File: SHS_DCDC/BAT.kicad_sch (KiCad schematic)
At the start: 15 parts, among them Q10 PMV100XPEAR, Q11 PMV100XPEAR, Q12 PMV100XPEAR, Q13 PMV100XPEAR, Q17 PMV100XPEAR, Q9 PMV100XPEAR, U2 INA181, U7 MCP101, U9 BD49LxxG

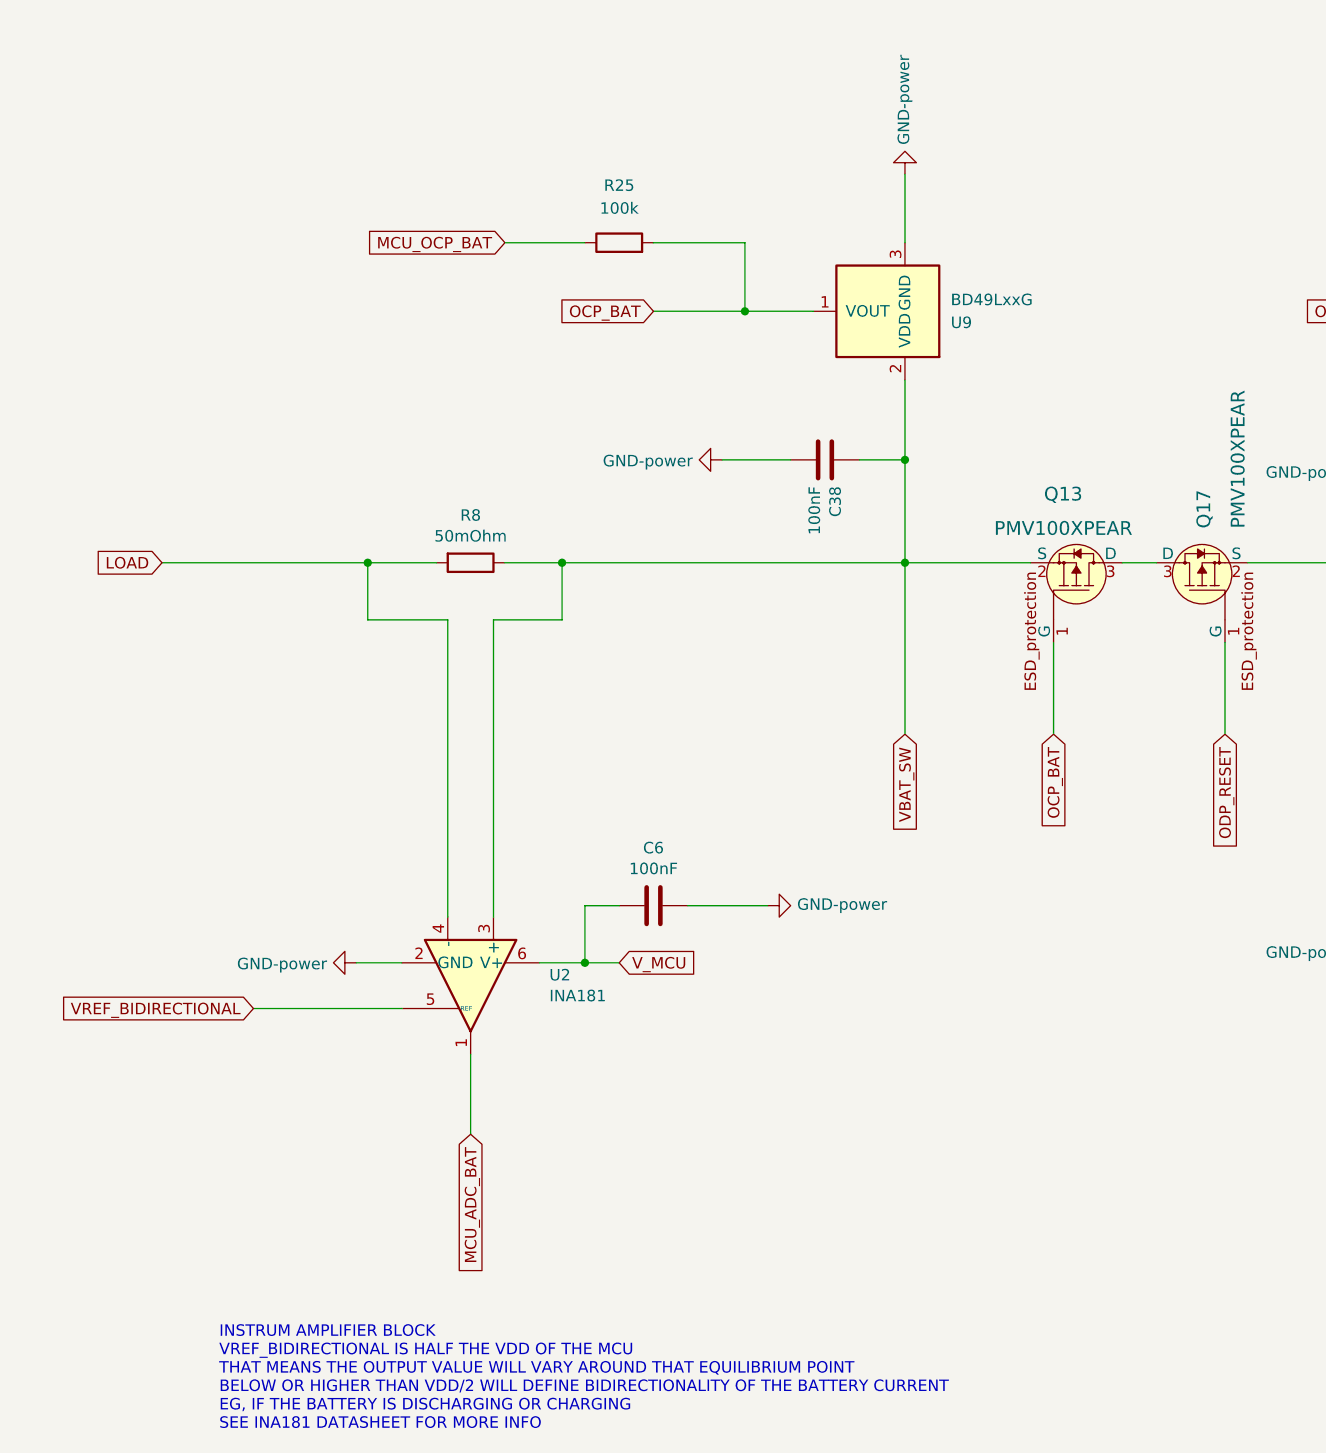
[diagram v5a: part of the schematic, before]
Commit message: 6 layers PCB
Decision to move to a 6 layers PCB to ease the PCB routing
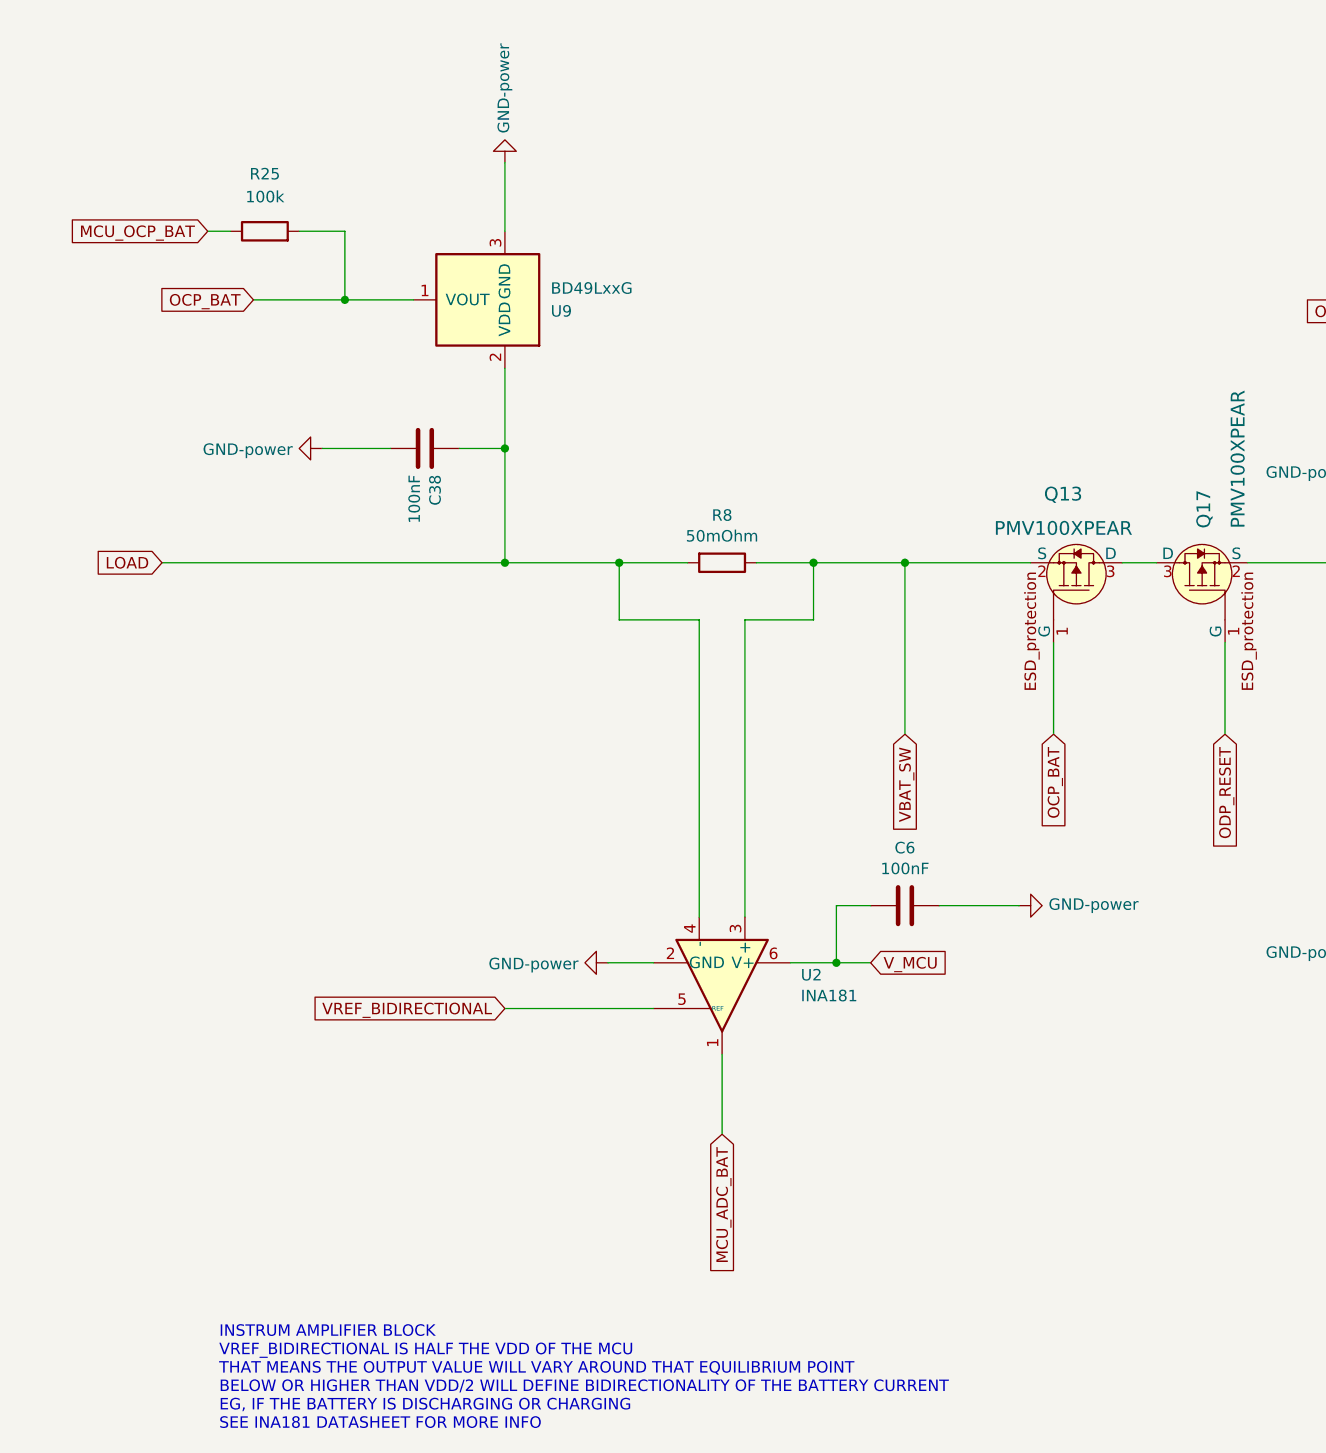
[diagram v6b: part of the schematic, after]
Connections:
- net LOAD: now also C38.1, U9.2 (VDD)
- net VBAT_SW: no longer C38.1, U9.2 (VDD)
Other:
- moved on the sheet: C38, C6, R25, R8, U2, U9

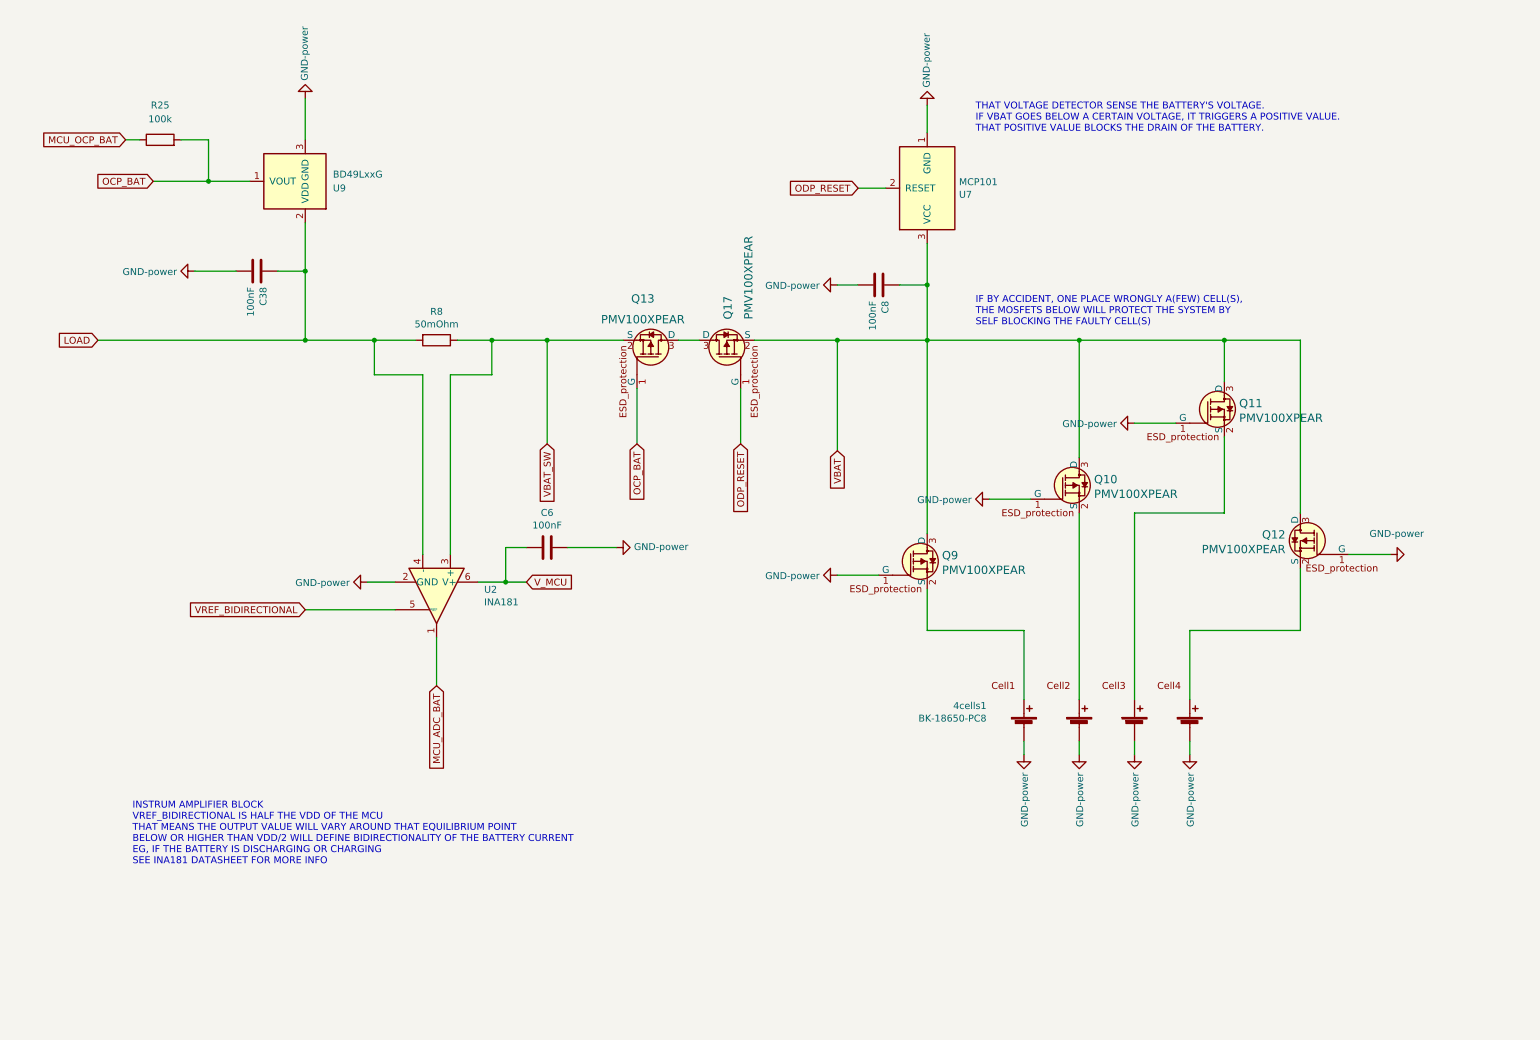
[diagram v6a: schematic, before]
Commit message: PV & BAT V sense
Adding 2 same blocks allowing the measure by ADC of the PV and Battery voltage on demand through power gating technique
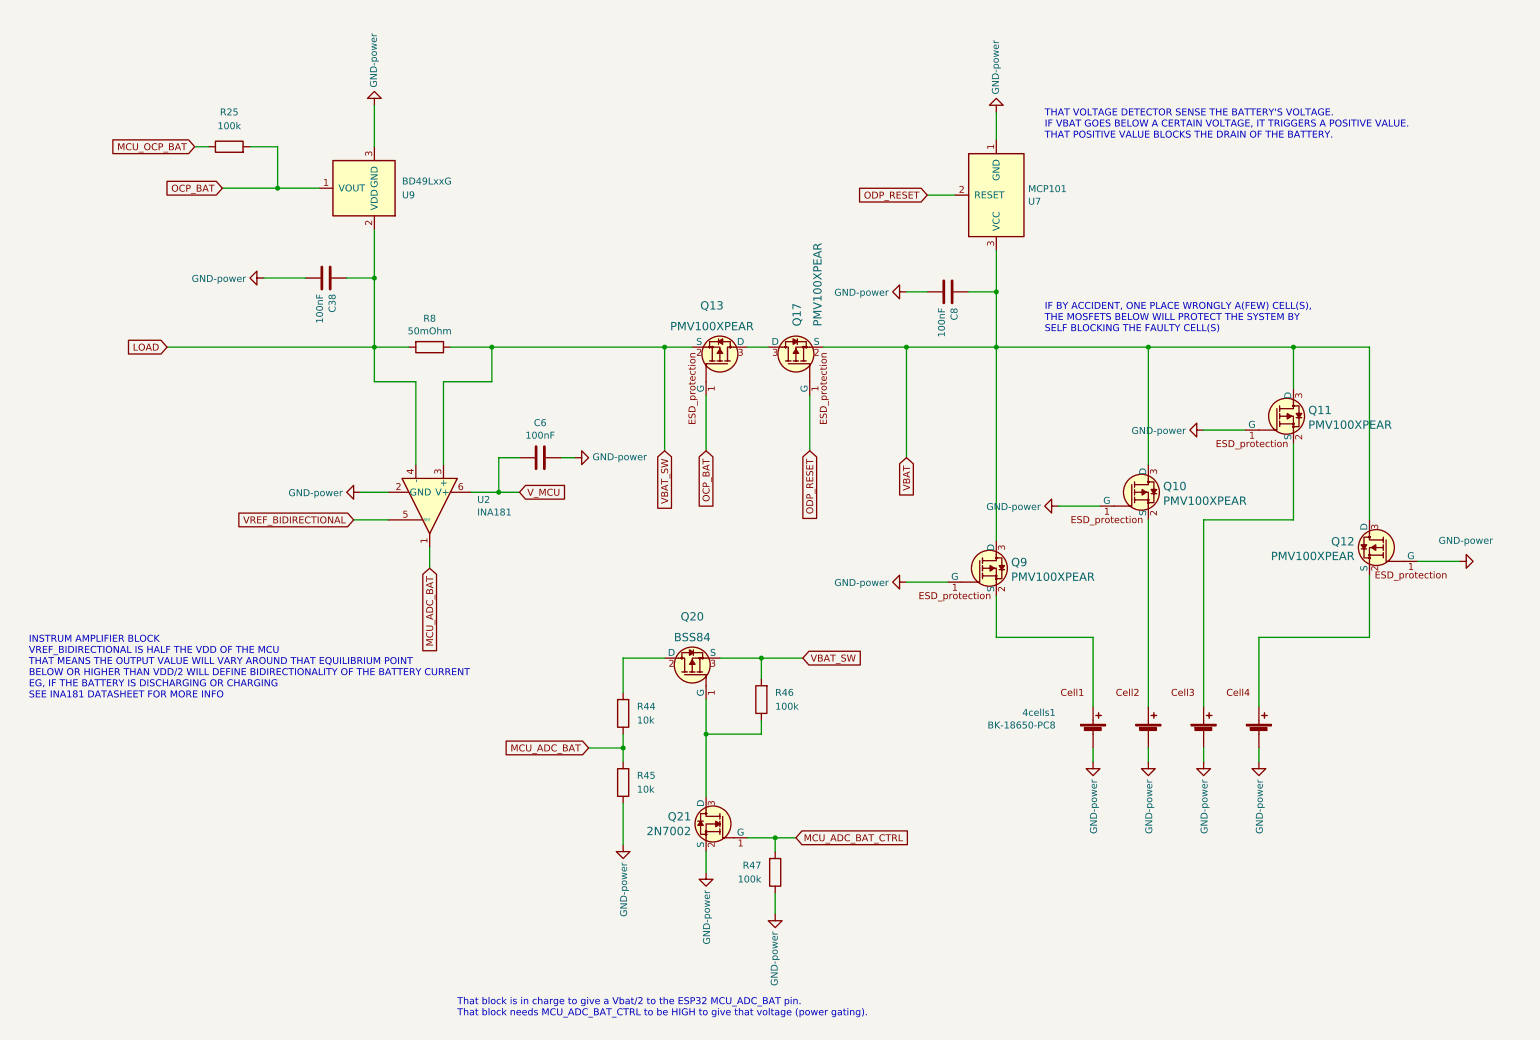
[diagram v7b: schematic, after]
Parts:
- added Q20: BSS84, Package_TO_SOT_SMD:SOT-23, symbol dk_Transistors-FETs-MOSFETs-Single:BSS84
- added Q21: 2N7002, Package_TO_SOT_SMD:SOT-23, symbol SHS_DCDC:2N7002-dk_Transistors-FETs-MOSFETs-Single
- added R44, R45: 10k, Resistor_SMD:R_0402_1005Metric, symbol Device:R
- added R46, R47: 100k, Resistor_SMD:R_0402_1005Metric, symbol Device:R
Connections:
- net GND: now also Q21.2 (S), R45.1, R47.1
- net MCU_ADC_BAT: now also R44.1, R45.2
- net VBAT_SW: now also Q20.3 (S), R46.2
- new net: Q20.1 (G), Q21.3 (D), R46.1
- new net: Q20.2 (D), R44.2
- new net MCU_ADC_BAT_CTRL: Q21.1 (G), R47.2
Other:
- note added: "That block is in charge to give a Vbat/2 to the ESP32 MCU_ADC_BAT pin. That block needs MCU_ADC_BAT_CTRL to be HIGH to give that voltage (power gating)."
- moved on the sheet: 4cells1, C38, C6, C8, Q10, Q11, Q12, Q13, Q17, Q9, R25, R8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

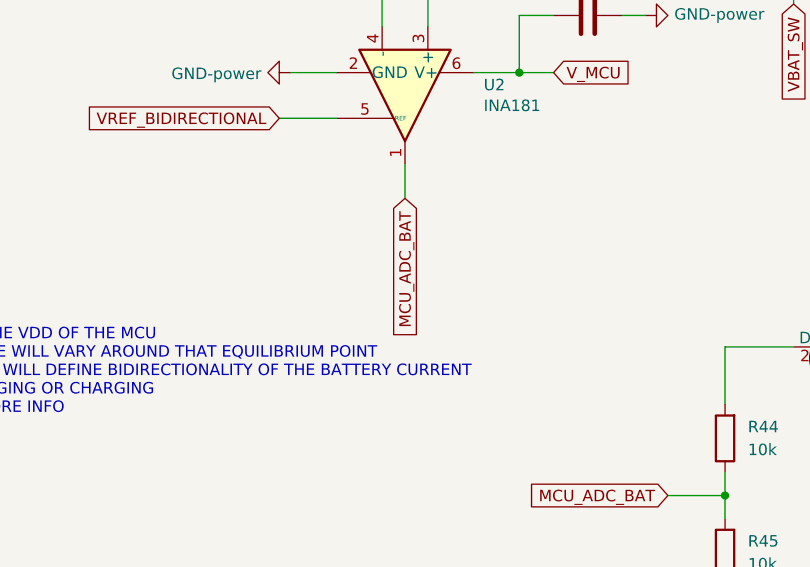
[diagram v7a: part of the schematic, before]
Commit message: ADC_PV & BAT
Blocks related to ADC reading of PV and BAT added on the physical board.
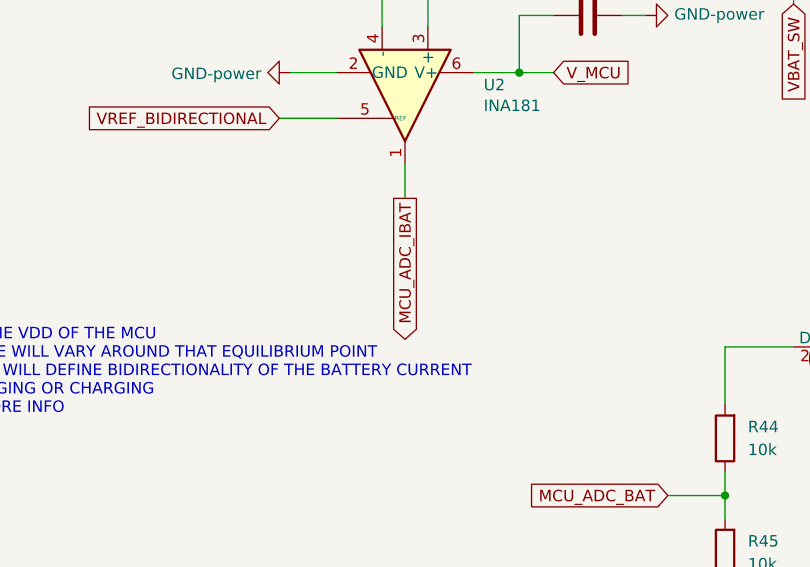
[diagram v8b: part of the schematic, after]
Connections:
- net MCU_ADC_BAT: no longer U2.1
- new net MCU_ADC_IBAT: U2.1
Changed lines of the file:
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@@
     )
   )
-  (global_label "MCU_ADC_BAT" (shape input) (at 86.36 113.03 270) (fields_autoplaced)
+  (global_label "MCU_ADC_IBAT" (shape output) (at 86.36 113.03 270) (fields_autoplaced)
     (effects (font (size 1.27 1.27)) (justify right))
-    (property "Intersheet References" "${INTERSHEET_REFS}" (id 0) (at -10.16 289.56 0)
-      (effects (font (size 1.27 1.27)) hide)
+    (property "Intersheet References" "${INTERSHEET_REFS}" (id 0) (at 86.2806 128.9009 90)
+      (effects (font (size 1.27 1.27)) (justify right) hide)
     )
   )
